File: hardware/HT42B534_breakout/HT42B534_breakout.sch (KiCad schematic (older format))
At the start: 17 parts, among them J1 USB-ID, J2 FTDI_PINS_1X06_input, U1 MCP1702-CB

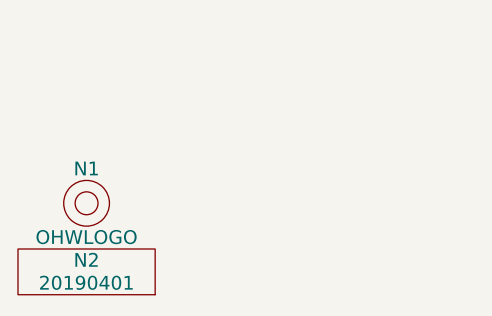
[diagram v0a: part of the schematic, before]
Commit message: changes paste aperatures, updated versionnumber
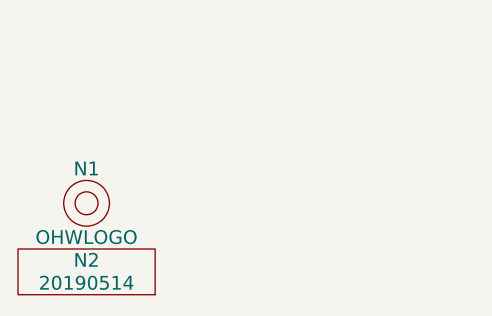
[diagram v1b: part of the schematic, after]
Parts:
- N2: value 20190401 -> 20190514
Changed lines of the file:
@@
 P 850 7700
 F 0 "N2" H 850 7800 60  0000 C CNN
-F 1 "20190401" H 850 7700 60  0000 C CNN
+F 1 "20190514" H 850 7700 60  0000 C CNN
 F 2 "SquantorLabels:Label_version" H 850 7700 60  0001 C CNN
 F 3 "" H 850 7700 60  0001 C CNN
